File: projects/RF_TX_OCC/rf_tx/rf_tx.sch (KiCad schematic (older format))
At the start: 15 parts, among them J1 Conn_01x03, J2 Conn_01x03, J3 Conn_01x04, J4 Conn_01x01_Female, SW1 SW_DIP_x08, SW2 SW_DIP_x04, U1 74LVC1G04, U2 74LVC1G14, U3 74LVC1G86, U4 HT12E

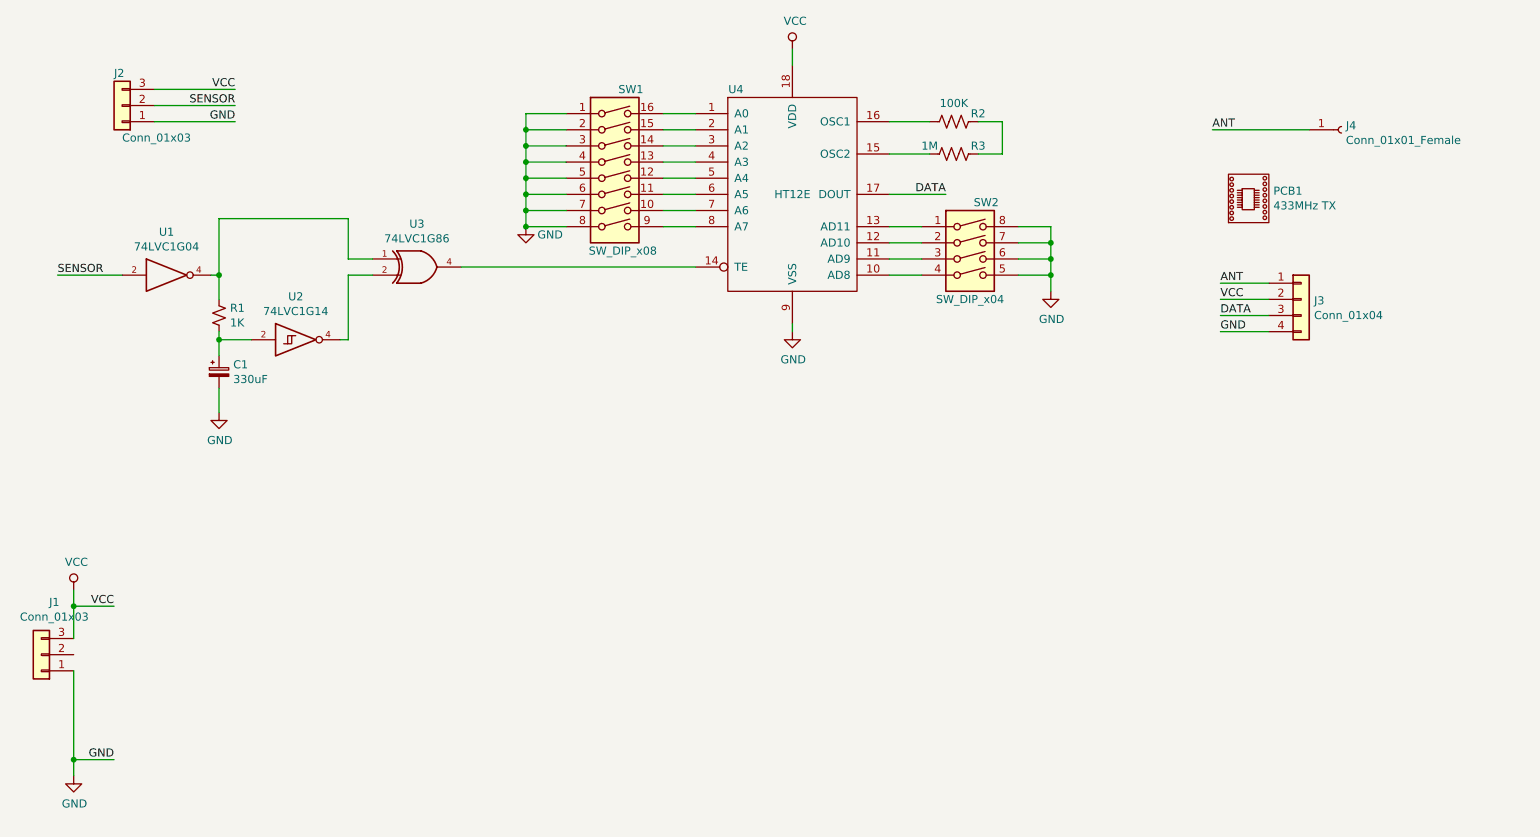
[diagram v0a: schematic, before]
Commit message: RF TX for the PIR sensor
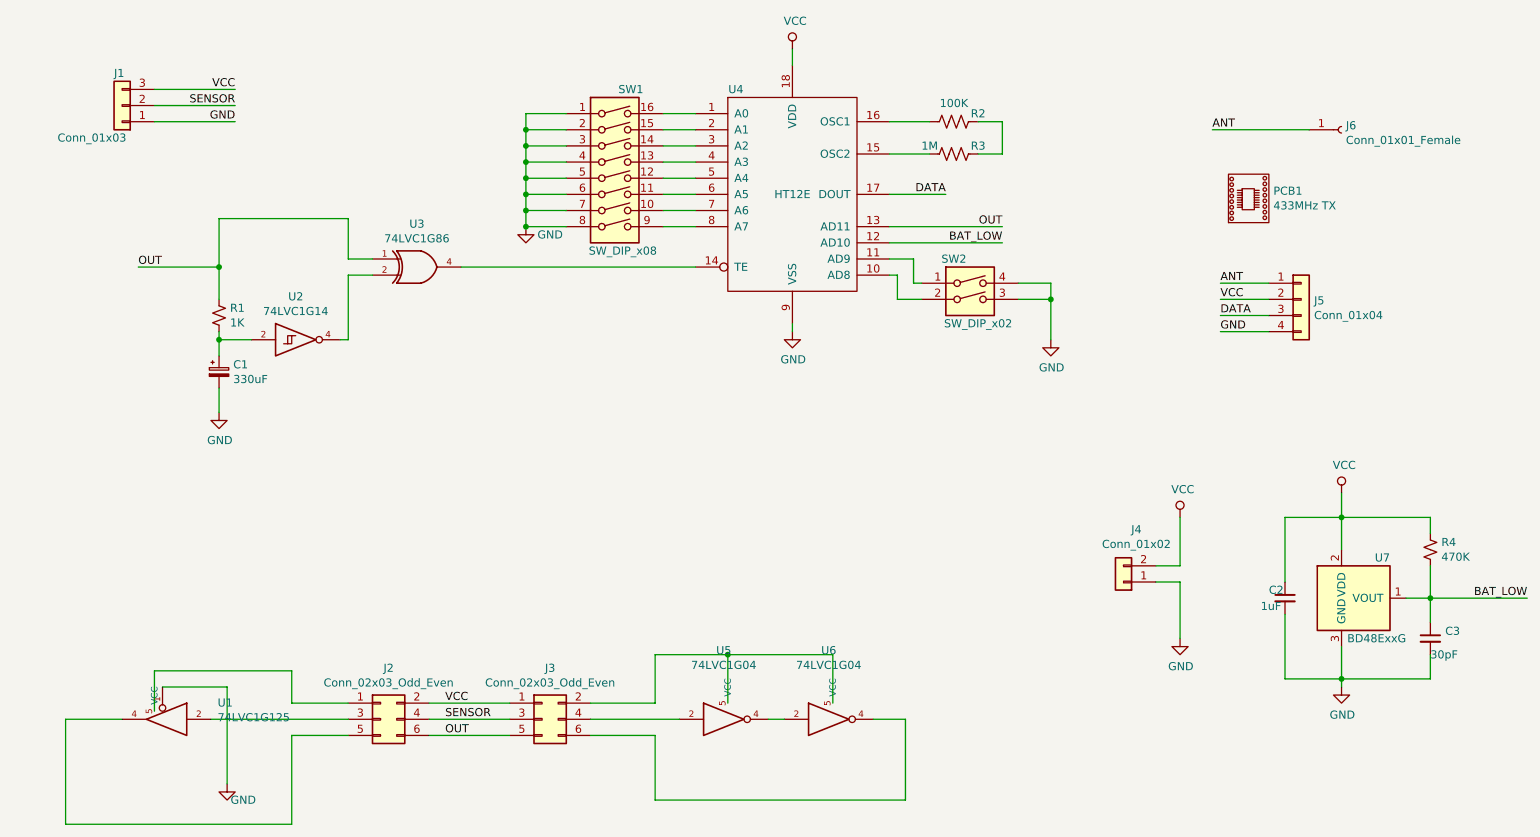
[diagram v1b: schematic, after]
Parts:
- removed J1: Conn_01x03, Connector_PinHeader_2.54mm:PinHeader_1x03_P2.54mm_Vertical, symbol Connector_Generic:Conn_01x03
- removed SW2: SW_DIP_x04, Package_DIP:DIP-8_W7.62mm_LongPads, symbol Switch:SW_DIP_x04
- removed U1: 74LVC1G04, Package_TO_SOT_SMD:SOT-23-5_HandSoldering, symbol 74xGxx:74LVC1G04
- added C2: 1uF, Capacitor_SMD:C_0805_2012Metric_Pad1.15x1.40mm_HandSolder, symbol Device:C_Small
- added C3: 30pF, Capacitor_SMD:C_0603_1608Metric_Pad1.05x0.95mm_HandSolder, symbol Device:C_Small
- added J2, J3: Conn_02x03_Odd_Even, Connector_PinHeader_2.54mm:PinHeader_2x03_P2.54mm_Vertical, symbol Connector_Generic:Conn_02x03_Odd_Even
- added J4: Conn_01x02, Connector_PinHeader_2.54mm:PinHeader_1x02_P2.54mm_Vertical, symbol Connector_Generic:Conn_01x02
- added R4: 470K, Resistor_SMD:R_0603_1608Metric_Pad1.05x0.95mm_HandSolder, symbol Device:R_Small_US
- added SW2: SW_DIP_x02, Package_DIP:DIP-4_W7.62mm_LongPads, symbol Switch:SW_DIP_x02
- added U1: 74LVC1G125, Package_TO_SOT_SMD:SOT-353_SC-70-5_Handsoldering, symbol hitesh_custom:74LVC1G125
- added U5: 74LVC1G04, Package_TO_SOT_SMD:SOT-23-5_HandSoldering, symbol hitesh_custom:74LVC1G04
- added U6: 74LVC1G04, Package_TO_SOT_SMD:TSOT-23-5_HandSoldering, symbol hitesh_custom:74LVC1G04
- added U7: BD48ExxG, Package_SO:TSOP-5_1.65x3.05mm_P0.95mm, symbol Power_Management:BD48ExxG
- U2: footprint Package_TO_SOT_SMD:SOT-23-5_HandSoldering -> Package_SO:TSOP-5_1.65x3.05mm_P0.95mm
- U3: footprint Package_TO_SOT_SMD:SOT-23-5_HandSoldering -> Package_TO_SOT_SMD:SOT-353_SC-70-5_Handsoldering
- renumbered J2 to J1, J3 to J5, J4 to J6
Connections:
- net GND: now also C2.2, C3.2, J4.1 (Pin_1), SW2.3, SW2.4, U1.1, U1.3 (GND), U5.3 (GND), U6.3 (GND), U7.3 (GND)
- net SENSOR: now also J2.4 (Pin_4), J3.3 (Pin_3)
- net VCC: now also C2.1, J2.2 (Pin_2), J3.1 (Pin_1), J4.2 (Pin_2), R4.1, U7.2 (VDD)
- net OUT: now reaches R1.1, U3.1
- net OUT: now also U4.13 (AD11), J2.6 (Pin_6), J3.5 (Pin_5)
- net at U4.10 (AD8): now also SW2.2
- net at U4.11 (AD9): now also SW2.1
- net BAT_LOW: now reaches U4.12 (AD10)
- net BAT_LOW: now also C3.1, R4.2, U7.1 (VOUT)
- new net: J2.1 (Pin_1), U1.5 (VCC)
- new net: J2.3 (Pin_3), U1.2
- new net: J2.5 (Pin_5), U1.4
- new net: J3.2 (Pin_2), U5.5 (VCC), U6.5 (VCC)
- new net: J3.4 (Pin_4), U5.2
- new net: J3.6 (Pin_6), U6.4
- new net: U5.4, U6.2
